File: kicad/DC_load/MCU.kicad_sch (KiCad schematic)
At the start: 125 parts, among them J1 BNC, J10 DC fan connector, J6 USB_B, J8 FT232 programming port, J9 Conn_01x04_Socket, Q1 MMBT5401, Q13 AO3400A, SW1 RotaryEncoder_Switch, SW2 RotaryEncoder_Switch, SW3 SW_Push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

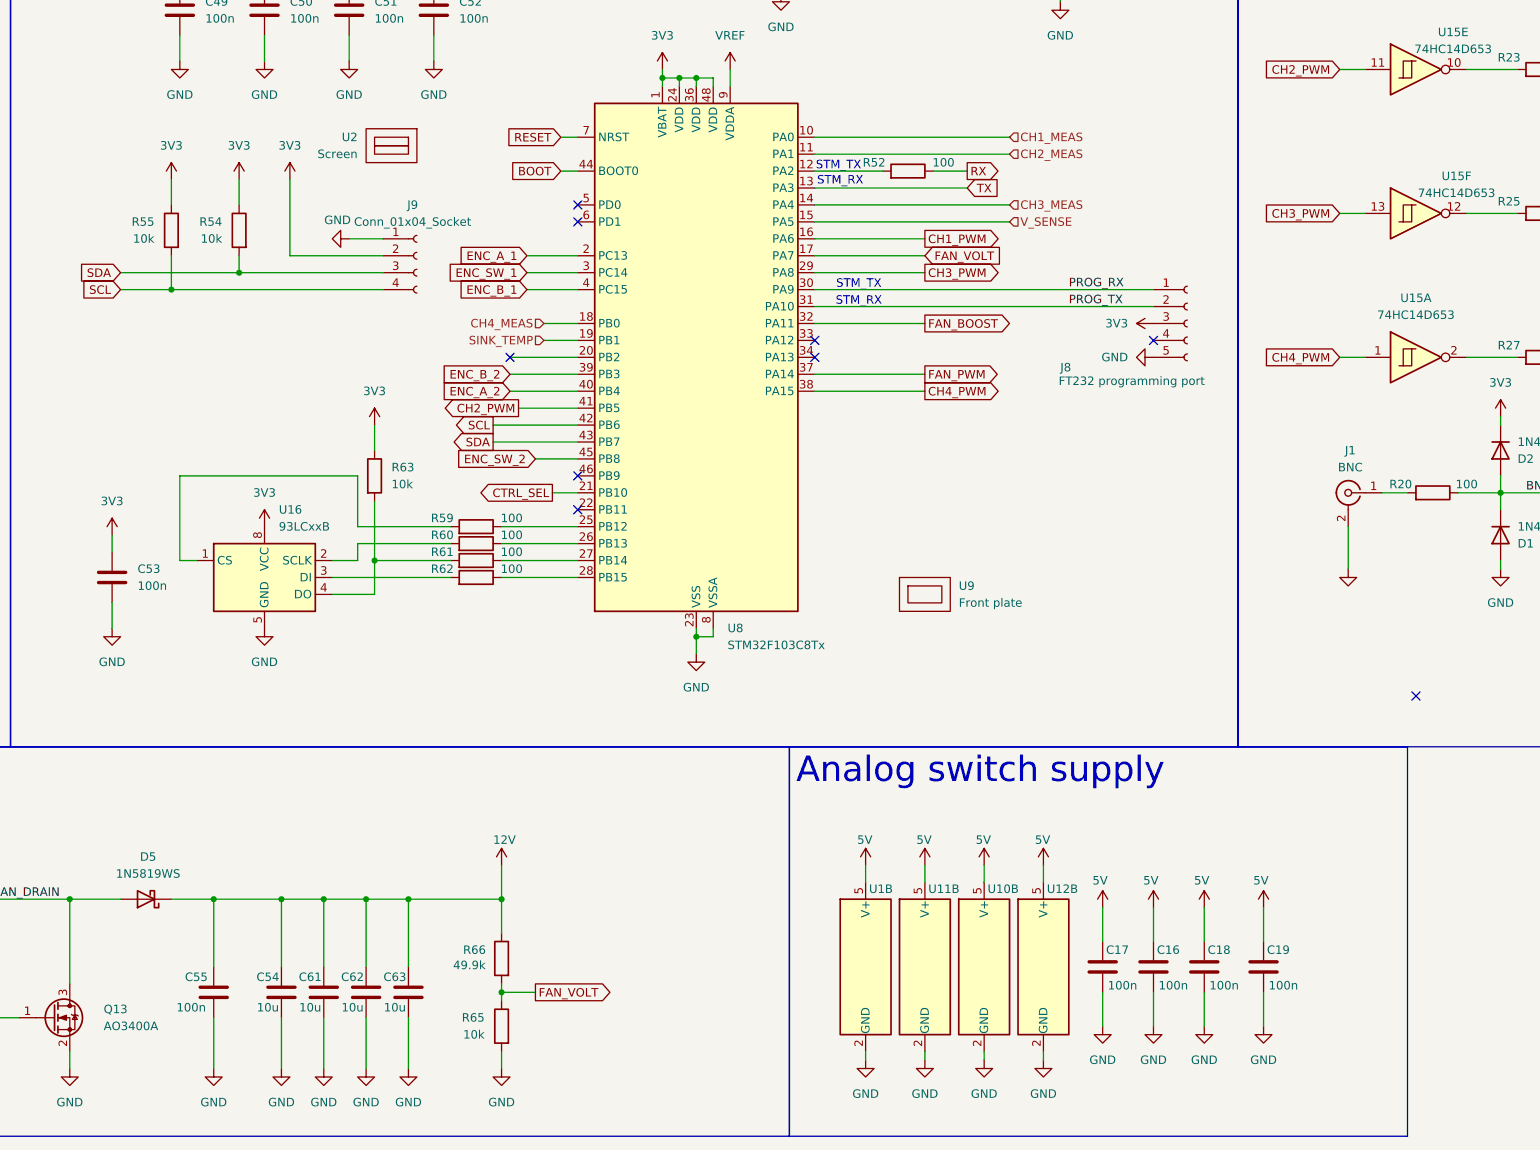
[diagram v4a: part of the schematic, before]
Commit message: RC filter na ADC linijama Placement update.
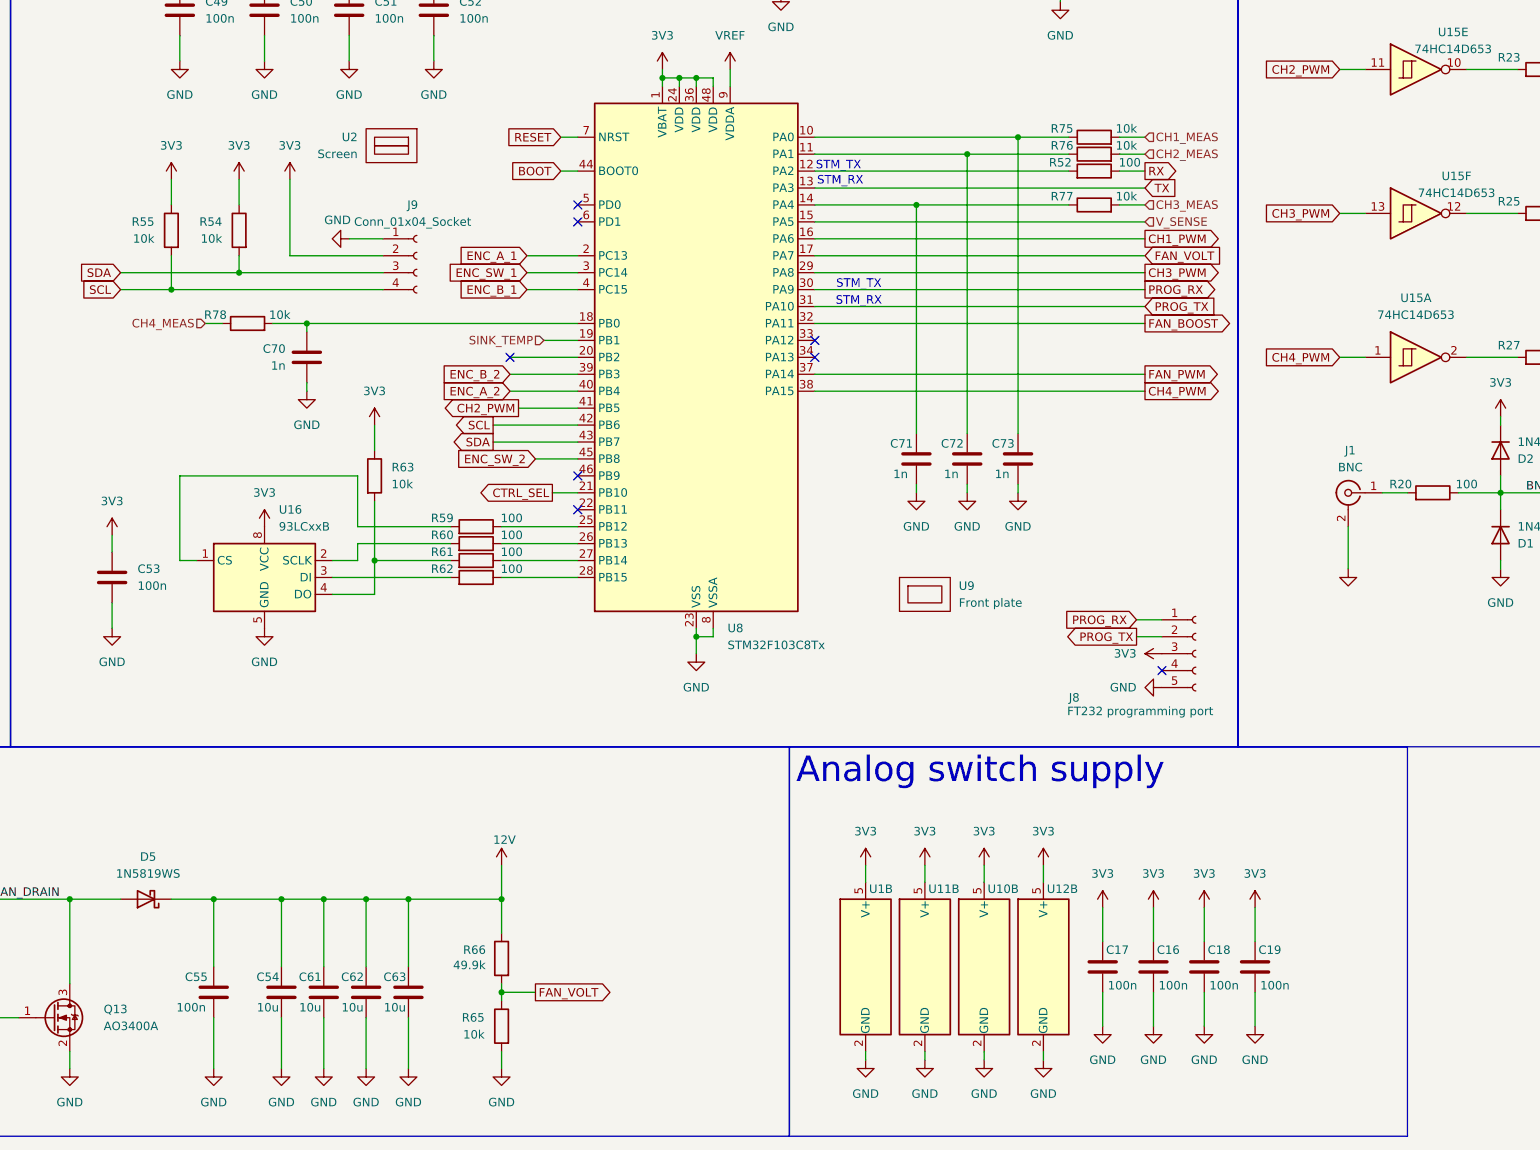
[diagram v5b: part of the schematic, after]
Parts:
- added C70, C71, C72, C73: 1n, Capacitor_SMD:C_0603_1608Metric_Pad1.08x0.95mm_HandSolder, symbol Device:C
- added R75, R76, R77, R78: 10k, Resistor_SMD:R_0603_1608Metric_Pad0.98x0.95mm_HandSolder, symbol Device:R
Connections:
- net 3V3: now also C16.2, C17.2, C18.2, C19.2, U1.5 (V+), U10.5 (V+), U11.5 (V+), U12.5 (V+)
- net 5V: no longer C16.2, C17.2, C18.2, C19.2, U1.5 (V+), U10.5 (V+), U11.5 (V+), U12.5 (V+)
- net CH1_MEAS: now also R75.2; no longer U8.10 (PA0)
- net CH2_MEAS: now also R76.2; no longer U8.11 (PA1)
- net CH3_MEAS: now also R77.2; no longer U8.14 (PA4)
- net CH4_MEAS: now also R78.1; no longer U8.18 (PB0)
- net GND: now also C70.1, C71.1, C72.1, C73.1
- new net: C70.2, R78.2, U8.18 (PB0)
- new net: C71.2, R77.1, U8.14 (PA4)
- new net: C73.2, R75.1, U8.10 (PA0)
- new net: C72.2, R76.1, U8.11 (PA1)
- no-connect marks 17 -> 16
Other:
- moved on the sheet: C19, J8, R52

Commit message: Done???.
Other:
- moved on the sheet: C21, C22, C23, C24, C25, C26, C27, C28, C54, C61, C62, C63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

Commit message: Ready for production.
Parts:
- removed U9: Front plate, DC_load:front_plate, symbol DC_load:front_plate
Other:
- title: (none) -> MCU sheet
- moved on the sheet: C36, C37, C38, C39, C40, C41, C70

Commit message: Sim, comp, power.
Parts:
- removed C54, C56, C58, C59, C60, C61, C62, C63: 10u, Capacitor_SMD:C_0603_1608Metric_Pad1.08x0.95mm_HandSolder, symbol Device:C
- removed C55: 100n, Capacitor_SMD:C_0603_1608Metric_Pad1.08x0.95mm_HandSolder, symbol Device:C
- removed D5: 1N5819WS, Diode_SMD:D_SOD-323, symbol Diode:1N5819WS
- removed L4: 4.7u, DC_load:L_Bourns_SRN6045TA, symbol solar_push_pull_sym_lib:SRN6045HA-4R7Y
- removed Q13: AO3400A, Package_TO_SOT_SMD:SOT-23, symbol Transistor_FET:AO3400A
- removed R65: 10k, Resistor_SMD:R_0603_1608Metric_Pad0.98x0.95mm_HandSolder, symbol Device:R
- removed R66: 49.9k, Resistor_SMD:R_0603_1608Metric_Pad0.98x0.95mm_HandSolder, symbol Device:R
- removed unit 2 of U15
- removed unit 3 of U15
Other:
- note removed: "Fan power supply"
